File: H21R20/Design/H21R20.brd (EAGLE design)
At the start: 34.6 x 30 mm, 40 parts, among them IC1 ESP32-C3-MINI-1-N4, P1 HEXABIT_17.32_NO_P6, X1 XTALL_CSTCE8M00G52

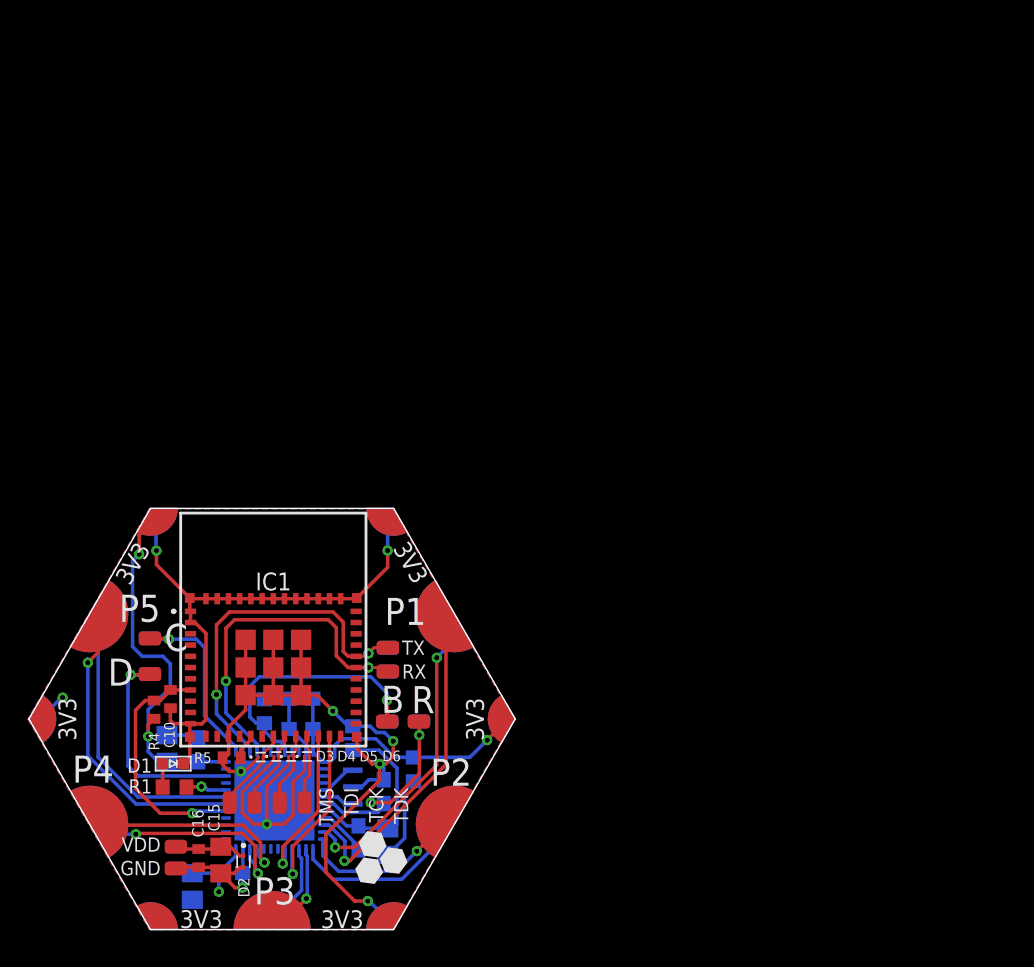
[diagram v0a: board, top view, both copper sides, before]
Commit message: -Changing the MC to STM32G0B1CEU6N -Changing the design of the hardware of the ESP32 circuit and the way it is connected to the MC,and adding test points to help with programming and debugging
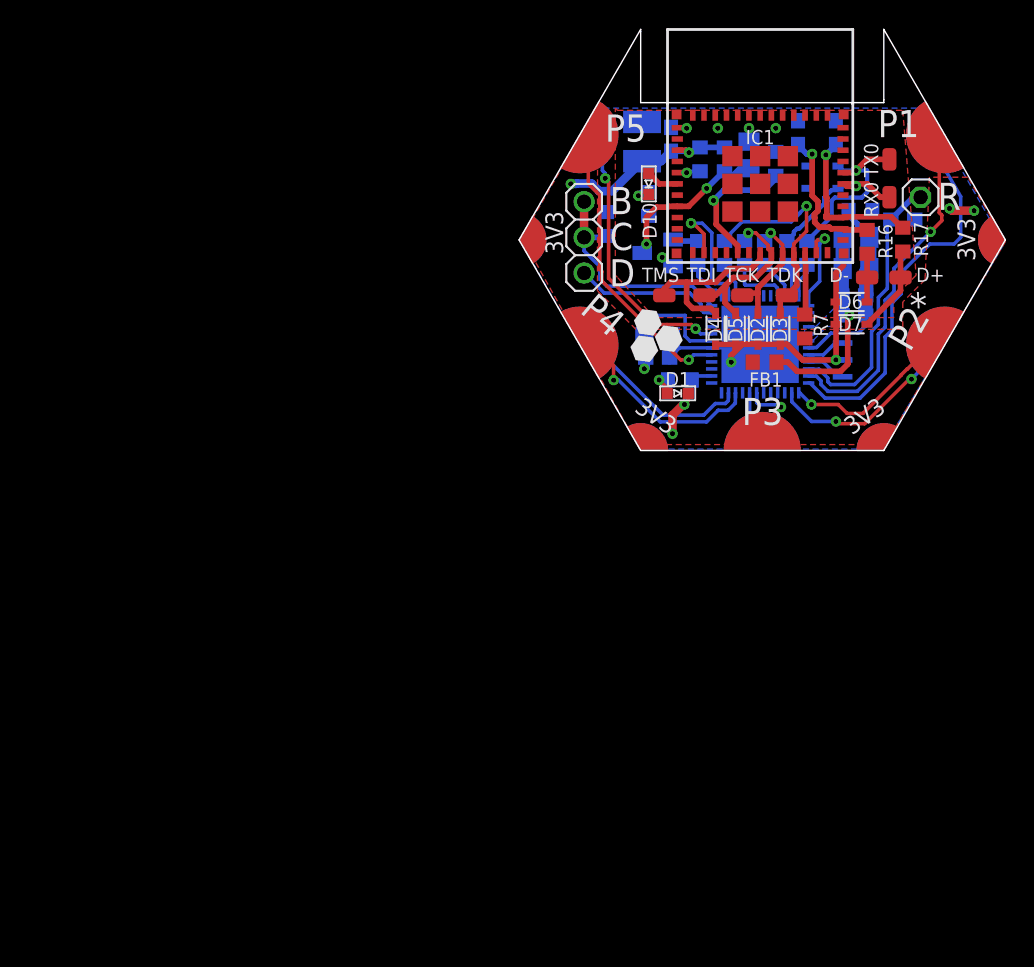
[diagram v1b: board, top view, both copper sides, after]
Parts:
- removed B, C, D, RX, TX: PAD1, Hexabitz:PAD1
- removed C15: 10uF, HEXABITZ_RCLS:C-0805
- removed C16: 0.1uF, HEXABITZ_RCLS:C-0402
- removed C2: 1.00uF, Hexabitz:C-0805-POL
- removed GND, VDD: PAD4, HEXABITZ_CONNECTION_PARTS:PAD4
- added C11: 47pF, HEXABITZ_RCLS:C-0603
- added C12: 100nF, HEXABITZ_RCLS:C-0603
- added C13: 10uF, HEXABITZ_RCLS:C-1210-POL
- added D+, D-, RX0, TX0: PAD4, HEXABITZ_CONNECTION_PARTS:PAD4
- added D10: RED, HEXABITZ_USER_INTERFACE_PARTS:VLMS1300-GS08
- added D7, D8, D9: BOURNS_CDSOD323-T03SCBOURNS_CDSOD323-T03SC_0_0, HEXABITZ_RCLS:BOURNS_CDSOD323-T03SC_0
- added JP1: (no value), pinhead:1X03
- added Q1: MMBT3904LT1, HEXABITZ_RCLS:MMBT3904LT1
- added R10, R14, R15, R7: 10K, HEXABITZ_RCLS:R-0603
- added R11, R12, R13, R8, R9: 0R, HEXABITZ_RCLS:R-0603
- added R16, R17: 27R, HEXABITZ_RCLS:R-0603
- C1: value 10nF -> 100nF; device Hexabitz:C-0603 -> HEXABITZ_RCLS:C-0603
- C10: value 0.1uF -> 47pF; device HEXABITZ_RCLS:C-0402 -> HEXABITZ_RCLS:C-0603
- C3, C8: value 100nF -> 4.7uF; device Hexabitz:C-0603 -> HEXABITZ_RCLS:C-0805-POL
- C4, C7: value 4.7uF -> 100nF; device Hexabitz:C-0805-POL -> HEXABITZ_RCLS:C-0603
- C5: device Hexabitz:C-0603 -> HEXABITZ_RCLS:C-0603
- C6, C9: value 100nF -> 1uF; device Hexabitz:C-0603 -> HEXABITZ_RCLS:C-0805-POL
- D1: value VLMS1300-GS08 -> RED; device Hexabitz:VLMS1300-GS08 -> HEXABITZ_USER_INTERFACE_PARTS:VLMS1300-GS08
- D2: value ESD9D5.0ST5G -> BOURNS_CDSOD323-T03SCBOURNS_CDSOD323-T03SC_0_0; device HEXABITZ_RCLS:TVS_ESD9D5.0ST5G -> HEXABITZ_RCLS:BOURNS_CDSOD323-T03SC_0
- D3, D4, D5, D6: value ESD7331MUT5G -> BOURNS_CDSOD323-T03SCBOURNS_CDSOD323-T03SC_0_0; device HEXABITZ_RCLS:DIODFN62X32X33-2N -> HEXABITZ_RCLS:BOURNS_CDSOD323-T03SC_0
- FB1: value FB-TDK_MMZ1608Y300B -> (none); device Hexabitz:FB-TDK_MMZ1608Y300B -> HEXABITZ_RCLS:FB-TDK_MMZ1608Y300B
- P1: value HEXABIT_17.32_NO_P6 -> HEXABIT_17.32_NO_P6_P7_P12; device hexabitz_connectors:HEXABIT_17.32_NO_P6 -> hexabitz_connectors:HEXABIT_17.32_NO_P6_P7_P12
- R: value PAD1 -> (none); device Hexabitz:PAD1 -> HEXABITZ_USER_INTERFACE_PARTS:1X01
- R1: value 270.0R -> 270R; device Hexabitz:R-0603 -> HEXABITZ_RCLS:R-0603
- R2: value 0.0R -> 10K; device Hexabitz:R-0603 -> HEXABITZ_RCLS:R-0603
- R3: value 10.0K -> 0.0R; device Hexabitz:R-0603 -> HEXABITZ_RCLS:R-0603
- R4: value 10k -> 270R; device HEXABITZ_RCLS:R-0402 -> HEXABITZ_RCLS:R-0603
- R5: value 100R -> 10K; device HEXABITZ_RCLS:R-0402 -> HEXABITZ_RCLS:R-0603
- U1: value (none) -> STM32G0B1CEU6NUFQFPN48_STM32_STM; device Hexabitz:STM32F091CBU6 -> HEXABITZ_ICs:UFQFPN48_STM32_STM
- X1: device Hexabitz:XTALL_CSTCE8M00G52 -> HEXABITZ_OTHER_PARTS:XTALL_CSTCE8M00G52
- moved C4 64.6 mm to (44.9, 35.6), turned to 0 degrees
- moved C10 62.3 mm to (40.2, 41.8), flipped to the bottom
- moved C5 60.5 mm to (41.4, 30.2), turned to 0 degrees
- moved C3 58.1 mm to (41.6, 32.1), turned to 180 degrees
- moved R3 55.5 mm to (41.9, 36.2), turned to 0 degrees
- moved R5 54.1 mm to (30.5, 39.8), flipped to the bottom, turned to 90 degrees
- moved D2 52.8 mm to (34.6, 27.8), turned to 90 degrees
- moved C9 51.9 mm to (34.0, 40.2), turned to 90 degrees
- moved R 51.7 mm to (46.2, 37.1), turned to 180 degrees
- moved C6 51.4 mm to (41.6, 34.3), turned to 180 degrees
- moved C1 51.3 mm to (41.4, 28.7), turned to 0 degrees
- moved D6 50.5 mm to (41.3, 29.7)
- moved R4 50.4 mm to (26.8, 36.7), flipped to the bottom, turned to 90 degrees
- moved C7 50.2 mm to (27.5, 25.7), turned to 0 degrees
- moved TDK 49.9 mm to (36.7, 30.2), turned to 0 degrees
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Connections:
- removed net B1: B.P$1, B.P$2, R3.2, U1.P$44
- removed net CHIP_EN: C10.1, IC1.8, R4.1, U1.P$29
- removed net ESP_BOOT: IC1.23, U1.P$16
- removed net ESP_MODE: IC1.22, U1.P$17
- removed net R1: C8.1, R.P$1, R.P$2, U1.P$7
- removed net UART1_RX: P1.PAD_PD5, U1.P$31
- removed net UART1_TX: P1.PAD_PU5, U1.P$30
- removed net UART2_RX: P1.PAD_PD2, U1.P$13
- removed net UART2_TX: P1.PAD_PU2, U1.P$12
- removed net UART3_RX: P1.PAD_PD4, U1.P$22
- removed net UART3_TX: P1.PAD_PU4, U1.P$21
- removed net UART4_RX: P1.PAD_PD1, U1.P$11
- removed net UART4_TX: P1.PAD_PU1, U1.P$10
- removed net UART5_RX: IC1.30, RX.P$1, RX.P$2, U1.P$40
- removed net UART5_TX: IC1.31, TX.P$1, TX.P$2, U1.P$39
- removed net UART6_RX: P1.PAD_PD3, U1.P$15
- removed net UART6_TX: P1.PAD_PU3, U1.P$14
- new net C: JP1.1, JP1.2, R2.2, U1.36
- new net D: JP1.3, U1.35
- new net DATA_N: C11.2, IC1.26, R16.1
- new net DATA_P: C10.2, IC1.27, R17.1
- new net D_N: D-.P$1, D6.2, R16.2
- new net D_P: D+.P$1, D7.2, R17.2
- new net ESP32_BOOT: IC1.23, U1.1
- new net ESP32_CS: IC1.13, U1.38
- new net ESP32_MISO: R13.2, U1.45
- new net ESP32_MOSI: R12.2, U1.46
- new net ESP32_RESET: R15.1, U1.37
- new net ESP32_RX0: R8.2, U1.47
- new net ESP32_SCK: R11.2, U1.39
- new net ESP32_TX0: R9.2, U1.48
- new net N$12: C4.2, R.1, U1.10
- new net N$13: Q1.1, R15.2
- new net N$14: D10.A, IC1.6
- new net N$15: IC1.5, R5.1
- new net N$17: R1.2, U1.26
- new net N$25: C9.1, IC1.8, Q1.3, R14.2
- new net N$4: IC1.22, R7.1
- new net USART1_RX: P1.PAD_PD5, U1.32
- new net USART1_TX: P1.PAD_PU5, U1.29
- new net USART2_RX: P1.PAD_PD2, U1.14
- new net USART2_TX: P1.PAD_PU2, U1.13
- new net USART3_RX: P1.PAD_PD4, U1.23
- new net USART3_TX: P1.PAD_PU4, U1.22
- new net USART4_RX: P1.PAD_PD1, U1.12
- new net USART4_TX: P1.PAD_PU1, U1.11
- new net USART5_RX: P1.PAD_PD3, U1.20
- new net USART5_TX: P1.PAD_PU3, U1.19
- net GND: now also C10.1, C11.1, C12.1, C13.2, C4.1, C7.1, D2.1, D7.1, D8.1, D9.1, Q1.2, R10.2, R4.1, U1.24, U1.25, U1.30, U1.49; no longer C10.2, C15.2, C16.2, C3.2, C4.2, C5.2, C6.2, C7.2, D2.2, GND.P$1, P1.PAD_PD12, P1.PAD_PD7, R5.1, U1.EP, U1.P$23, U1.P$35, U1.P$47
- net N$1: now also U1.8, X1.P$1; no longer D3.2, IC1.18, TMS.P$1
- net N$10: now also D3.2, R11.1; no longer D6.2
- net N$11: now also D5.2, IC1.19, R13.1, TDI.P$1; no longer IC1.16, R5.2
- net N$2: now also U1.9, X1.P$3; no longer D4.2, IC1.19, TDI.P$1
- net N$3: now also D4.2, IC1.18, TMS.P$1; no longer R1.2, U1.P$32
- net N$5: now also D10.C, R4.2; no longer U1.P$5, X1.P$1
- net N$6: now also D8.2, IC1.30, R8.1, RX0.P$1; no longer U1.P$6, X1.P$3
- net N$7: now also D9.2, IC1.31, R9.1, TX0.P$1; no longer D.P$1, D.P$2, U1.P$34
- net N$8: now also D2.2, R12.1; no longer D5.2
- net N$9: now also IC1.16, R10.1; no longer C.P$1, C.P$2, U1.P$37
- net VDD: now also C12.2, C13.1, C7.2, C8.1, FB1.1, R14.1, R5.2, R7.2, U1.31; no longer C15.1, C16.1, C3.1, C4.1, C5.1, C6.1, C7.1, C9.1, D2.1, FB1.2, P1.PAD_PU12, P1.PAD_PU7, R4.2, U1.P$1, U1.P$24, U1.P$36, U1.P$48, VDD.P$1
- net VDDA: now also C1.2, C3.1, C5.2, C6.1, FB1.2, U1.4, U1.5, U1.6; no longer C1.1, C2.1, FB1.1, U1.P$9
- net VSSA: now also C1.1, C3.2, C5.1, C6.2, R3.2, U1.7; no longer C1.2, C2.2, R2.2, U1.P$8
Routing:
- net GND: track 151.8 -> 31.8 mm, vias 10 -> 11
- net VDD: track 58.7 -> 25.2 mm, vias 4 -> 3
- net USART4_RX: track 0.00 -> 27.0 mm
- net UART5_TX: track 27.0 -> 0.00 mm, vias 2 -> 0
- net UART5_RX: track 25.7 -> 0.00 mm, vias 2 -> 0
- net USART4_TX: track 0.00 -> 24.7 mm, vias 0 -> 1
- net UART4_TX: track 23.9 -> 0.00 mm, vias 1 -> 0
- net UART4_RX: track 22.0 -> 0.00 mm, vias 2 -> 0
- net UART1_TX: track 21.3 -> 0.00 mm, vias 1 -> 0
- net USART1_TX: track 0.00 -> 20.8 mm, vias 0 -> 1
- net B1: track 20.4 -> 0.00 mm, vias 1 -> 0
- net UART1_RX: track 20.2 -> 0.00 mm
- net N$12: track 0.00 -> 20.1 mm
- net USART1_RX: track 0.00 -> 19.6 mm, vias 0 -> 2
- net CHIP_EN: track 17.4 -> 0.00 mm, vias 1 -> 0
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- added copper zone on layer 1, net GND
- added copper zone on layer 16, net VDDA
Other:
- outline, holes or cut-outs redrawn
- board text added: "*"
- board text added: "P2*"
- board text removed: "P2"
- board text removed: "RX"
- board text removed: "TX"

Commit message: -Changing some issues in the design to improve the performance
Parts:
- removed C9: 1uF, HEXABITZ_RCLS:C-0805-POL
- removed Q1: MMBT3904LT1, HEXABITZ_RCLS:MMBT3904LT1
- removed R15: 10K, HEXABITZ_RCLS:R-0603
- added C2: 100nF, HEXABITZ_RCLS:C-0603
- X1: value XTALL_CSTCE8M00G52 -> 8MHZ
- moved C10 11.0 mm to (44.0, 31.4), flipped to the top, turned to 180 degrees
- moved C11 10.8 mm to (40.8, 31.4), flipped to the top, turned to 0 degrees
- moved R10 10.4 mm to (32.5, 29.7), flipped to the top, turned to 270 degrees
- moved R14 10.2 mm to (31.1, 29.7), flipped to the top, turned to 90 degrees
- moved D6 6.37 mm to (40.8, 23.3), turned to 90 degrees
- moved D+ 6.08 mm to (42.7, 25.7)
- moved D- 5.93 mm to (40.8, 25.7)
- moved D4 5.39 mm to (27.9, 23.8)
- moved R2 5.39 mm to (27.6, 31.4)
- moved D2 5.29 mm to (31.1, 23.8)
- moved D5 5.29 mm to (29.5, 23.8)
- moved D3 5.29 mm to (32.7, 23.8)
- moved R17 5.22 mm to (43.2, 29.2)
- moved R16 5.07 mm to (40.6, 29.2)
- moved D7 4.97 mm to (42.7, 23.3), turned to 90 degrees
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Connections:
- removed net N$11 (its old number): D5.2, IC1.19, R13.1, TDI.P$1
- removed net N$13: Q1.1, R15.2
- removed net N$25: C9.1, IC1.8, Q1.3, R14.2
- removed net N$8: D2.2, IC1.20, R12.1, TCK.P$1
- removed net USART3_RX: P1.PAD_PD4, U1.23
- removed net USART3_TX: P1.PAD_PU4, U1.22
- new net N$10: D2.2, IC1.20, R13.1, TCK.P$1
- new net N$18: D5.2, IC1.19, R12.1, TDI.P$1
- new net USART6_RX: P1.PAD_PD3, U1.16
- new net USART6_TX: P1.PAD_PU3, U1.15
- net ESP32_CS: now also U1.37; no longer U1.38
- net ESP32_MISO: now also U1.43; no longer U1.45
- net ESP32_MOSI: now also U1.44; no longer U1.46
- net ESP32_RESET: now also C2.2, IC1.8, R14.2, U1.38; no longer R15.1, U1.37
- net ESP32_SCK: now also U1.42; no longer U1.39
- net GND: now also C2.1, U1.2, U1.23, U1.3; no longer C9.2, Q1.2
- net N$6: now also D9.2; no longer D8.2
- net N$7: now also D8.2; no longer D9.2
- net USART1_RX: now also P1.PAD_PD4; no longer P1.PAD_PD5
- net USART1_TX: now also P1.PAD_PU4; no longer P1.PAD_PU5
- net USART5_RX: now also P1.PAD_PD5, U1.40; no longer P1.PAD_PD3, U1.20
- net USART5_TX: now also P1.PAD_PU5, U1.41; no longer P1.PAD_PU3, U1.19
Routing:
- net GND: track 31.8 -> 99.9 mm, vias 11 -> 34
- net VDD: track 25.2 -> 79.1 mm, vias 3 -> 2
- net N$10: track 0.00 -> 20.4 mm, vias 0 -> 1
- net N$18: track 0.00 -> 17.1 mm, vias 0 -> 1
- net USART3_TX: track 14.8 -> 0.00 mm, vias 1 -> 0
- net USART5_RX: track 3.79 -> 17.6 mm
- net USART3_RX: track 13.2 -> 0.00 mm
- net ESP32_RESET: track 3.08 -> 15.9 mm, vias 0 -> 1
- net USART5_TX: track 5.52 -> 17.7 mm
- net N$11 (its old number): track 11.8 -> 0.00 mm, vias 1 -> 0
- net N$25: track 11.8 -> 0.00 mm, vias 2 -> 0
- net N$8: track 9.02 -> 0.00 mm, vias 1 -> 0
- net USART1_TX: track 20.8 -> 11.8 mm
- net N$11: track 15.6 -> 23.7 mm
- net USART6_TX: track 0.00 -> 7.81 mm, vias 0 -> 1
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
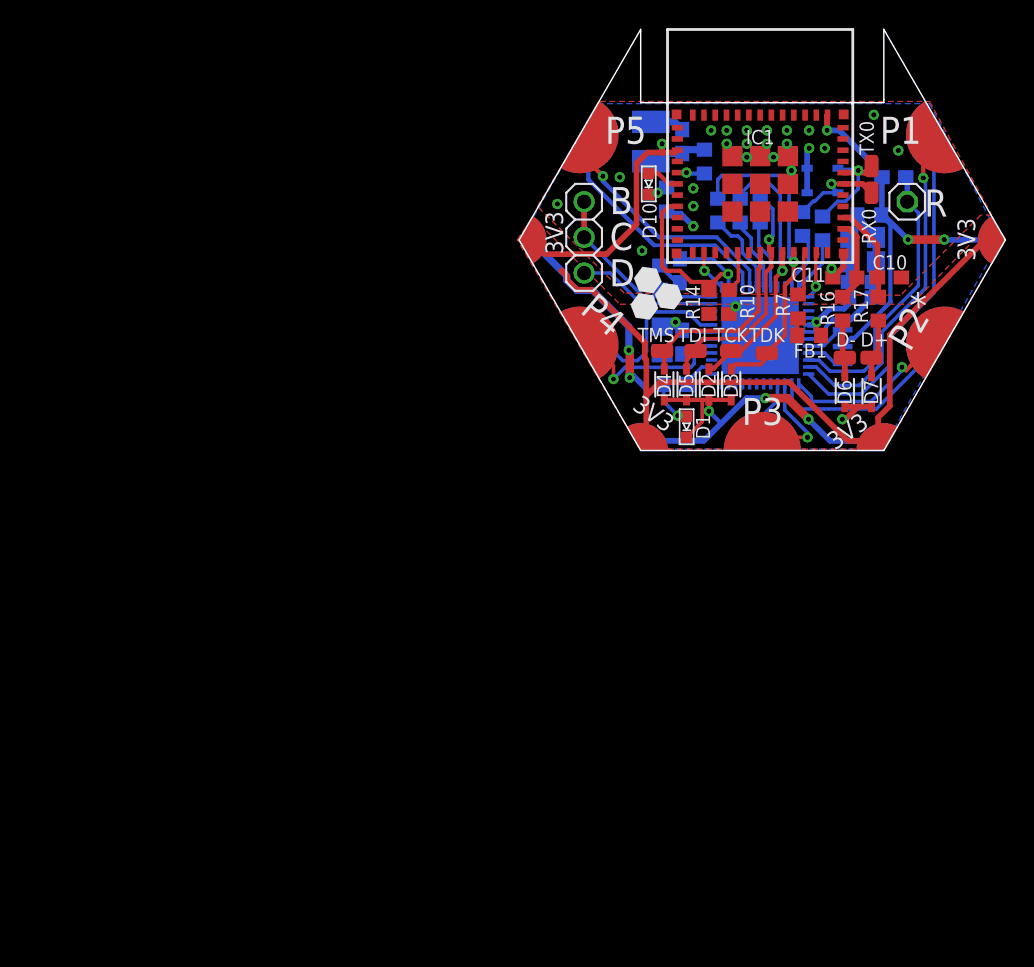
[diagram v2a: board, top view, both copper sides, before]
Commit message: -Changing the placement of the ESP32
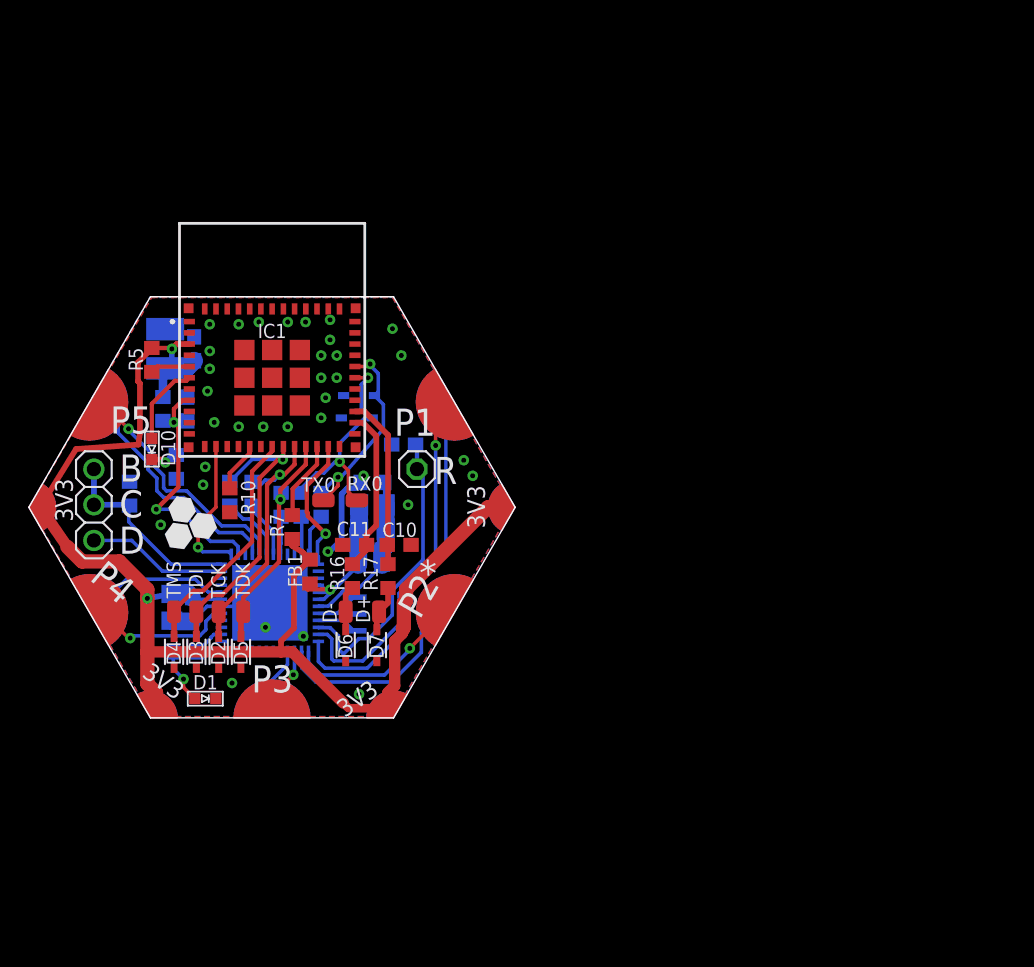
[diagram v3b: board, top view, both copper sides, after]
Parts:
- moved TX0 45.7 mm to (3.65, 15.6), turned to 0 degrees
- moved RX0 42.7 mm to (6.03, 15.6), turned to 180 degrees
- moved D3 42.6 mm to (-5.40, 4.76)
- moved R5 41.8 mm to (-8.57, 25.6), flipped to the top
- moved TDK 41.6 mm to (-2.06, 7.62), turned to 90 degrees
- moved TCK 41.0 mm to (-3.81, 7.62), turned to 90 degrees
- moved R8 40.9 mm to (2.06, 15.2)
- moved R2 40.8 mm to (-10.2, 16.0)
- moved R9 40.8 mm to (3.49, 15.2)
- moved R3 40.2 mm to (7.14, 16.8), turned to 180 degrees
- moved R11 40.2 mm to (-3.02, 16.0)
- moved R13 40.2 mm to (-1.43, 16.0)
- moved D10 40.1 mm to (-8.57, 19.2)
- moved TDI 40.1 mm to (-5.40, 7.62), turned to 270 degrees
- moved R12 40.1 mm to (0.64, 15.2)
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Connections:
- net N$11: now also D5.2, R12.1; no longer D3.2, R11.1
- net N$18: now also D3.2, R11.1; no longer D5.2, R12.1
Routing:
- net GND: track 99.9 -> 13.8 mm
- net VDD: track 79.1 -> 97.4 mm
- net N$6: track 7.05 -> 15.9 mm, vias 1 -> 2
- net N$11: track 23.7 -> 15.9 mm
- net ESP32_CS: track 3.02 -> 10.3 mm
- net N$7: track 8.55 -> 15.1 mm, vias 1 -> 2
- net ESP32_BOOT: track 3.50 -> 9.83 mm
- net DATA_N: track 5.93 -> 11.8 mm
- net DATA_P: track 6.98 -> 12.3 mm
- net N$18: track 17.1 -> 21.2 mm
- net VDDA: track 9.32 -> 13.0 mm
- net N$14: track 2.35 -> 5.91 mm
- net N$3: track 13.6 -> 16.9 mm
- net USART6_TX: track 7.81 -> 4.77 mm
- net ESP32_RESET: track 15.9 -> 18.7 mm, vias 1 -> 2
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- removed copper zone on layer 1, net VDD
- removed copper zone on layer 16, net VDDA
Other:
- outline, holes or cut-outs redrawn
- board text removed: "*"
